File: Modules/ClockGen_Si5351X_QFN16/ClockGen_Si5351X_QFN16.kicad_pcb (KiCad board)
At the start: 4 copper layers, 66.8 x 38.1 mm, 112 parts, among them J1 Screw Terminal, J10 2.54mm Stackable Socket, J11 2.54mm Stackable Socket, J12 2.54mm Stackable Socket, J13 2.54mm Stackable Socket, J14 2.54mm Stackable Socket, J2 JST SH, J3 SMA, J4 2.54 Pins, J5 2.54 Pins, J6 SMA, J7 SMA, J8 SMA, J9 SMA, Q1 GSFJ0300, Q2 GSFK0502, SW1 SW_SPDT, U1 NCV68061, U2 NCV68061, U3 TPS7E8201, U4 SI5351B-B-GM1, U5 AP2127K-ADJ, U6 LM66200, Y1 25MHz

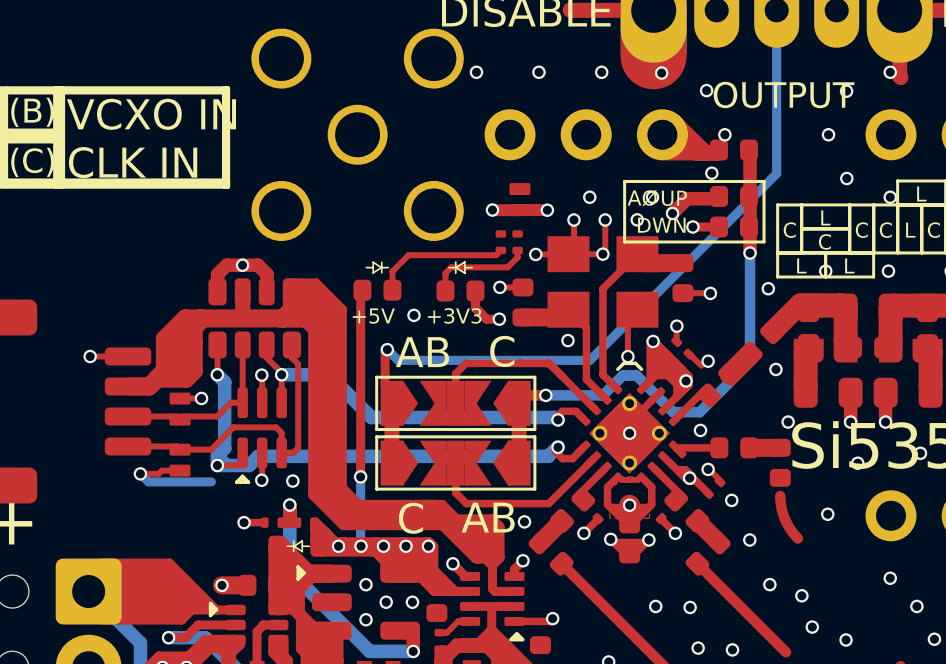
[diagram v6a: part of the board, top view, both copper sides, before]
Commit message: Replaced Q2 with GSFJ0300
Lower Rds, smaller footprint, parts commonality with Q1
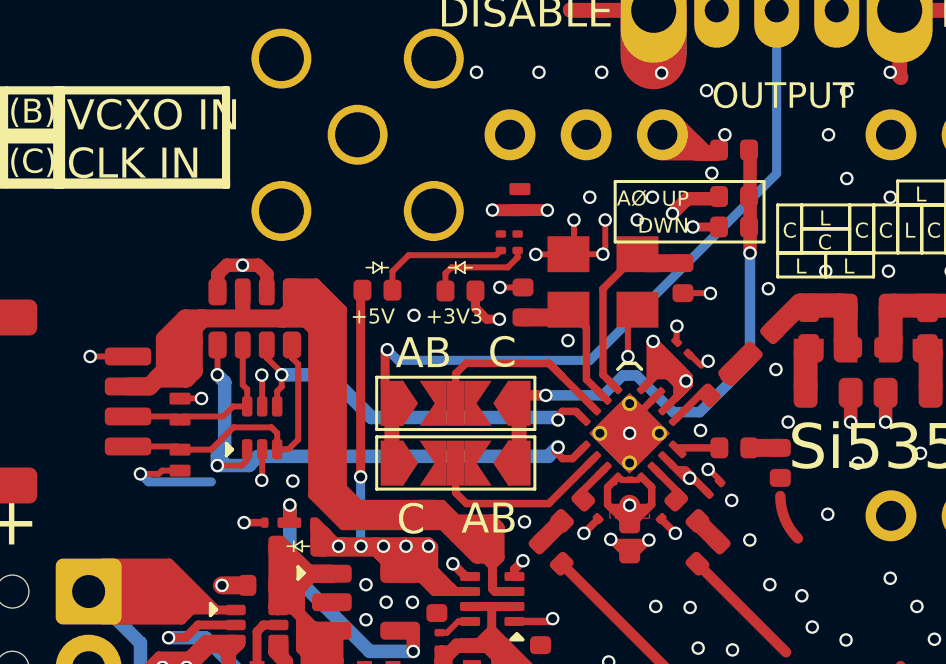
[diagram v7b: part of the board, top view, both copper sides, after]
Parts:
- Q2: value GSFK0502 -> GSFJ0300; footprint Package_TO_SOT_SMD:SOT-363_SC-70-6 -> Package_TO_SOT_SMD:SOT-563
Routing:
- net /I2C_SDA: track 18.7 -> 19.3 mm

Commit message: Silkscreen art added
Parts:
- added G***: LOGO, libraries:Logo_15mm_inv, B.Cu at (153.2, 102.1)
- moved D1 4.32 mm to (148.9, 87.2), turned to -90 degrees
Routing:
- net GND: track 84.0 -> 82.2 mm, vias 166 -> 167
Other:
- board text added: "CLK0"
- board text added: "CLK1"
- board text added: "CLK2"
- board text added: "CLK3"
- board text added: "CLOCK 0"
- board text added: "CLOCK 1"
- board text added: "CLOCK 2"
- board text added: "CLOCK 3"
- board text added: "Rev A"
- board text added: "Si5351[X]"
- board text added: "VCXO CLK"
- board text removed: "Si5351"
